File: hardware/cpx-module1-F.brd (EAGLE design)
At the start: 85.1 x 128.5 mm, 6 parts, among them T1 TOUCHPADROUND1, T2 TOUCHPADROUND1, T3 TOUCHPADROUND1, T4 TOUCHPADROUND1, U1 CIRCUITPLAYGROUNDEXPRESS

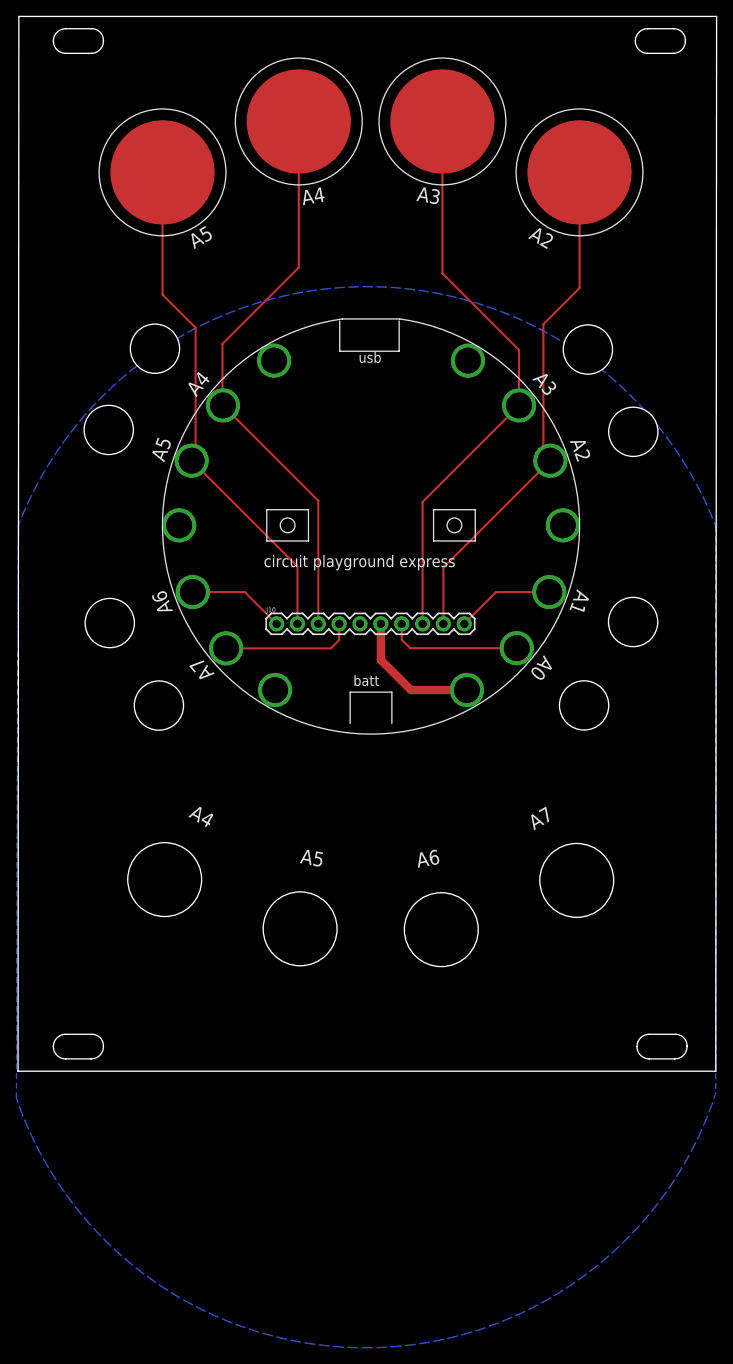
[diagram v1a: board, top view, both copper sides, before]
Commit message: added protection diodes and filter caps, added pdfs
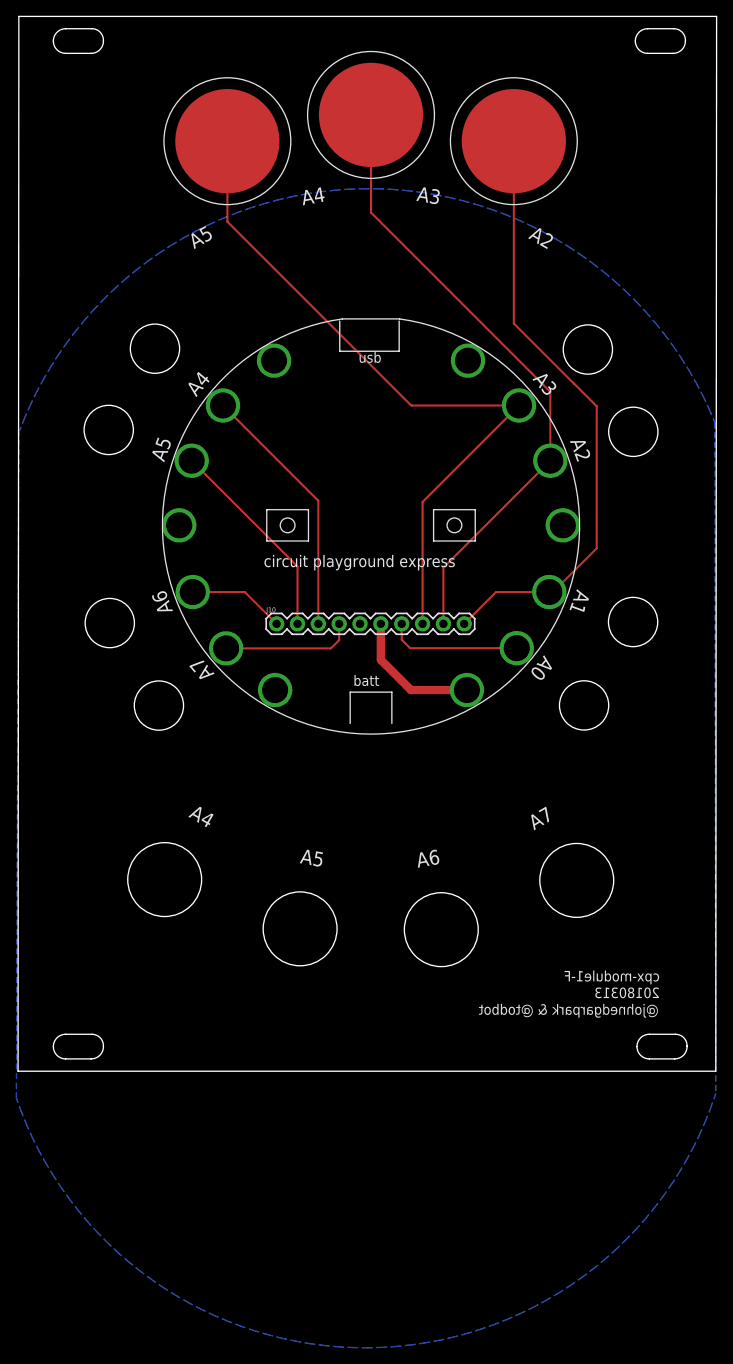
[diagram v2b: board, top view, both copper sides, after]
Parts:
- removed T3: TOUCHPADROUND1, todstuff:TOUCHPAD1
- moved T2 43.0 mm to (17.4, 50.8)
- moved T4 26.3 mm to (0.00, 54.0)
- moved T1 26.3 mm to (-17.5, 50.8)
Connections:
- net A1: now also T2.TOUCH
- net A4: no longer T3.TOUCH
- net A5: no longer T2.TOUCH
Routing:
- net A1: track 12.0 -> 73.7 mm
- net A4: track 69.9 -> 31.4 mm
- net A5: track 62.3 -> 25.2 mm
- net A3: track 69.9 -> 86.1 mm
- net A2: track 62.6 -> 76.4 mm
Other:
- board text added: "20180313"
- board text added: "@johnedgarpark & @todbot"
- board text added: "cpx-module1-F"
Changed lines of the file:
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@@
 <layer number="131" name="prix" color="7" fill="1" visible="no" active="yes"/>
 <layer number="132" name="test" color="7" fill="1" visible="no" active="yes"/>
+<layer number="133" name="Ports" color="7" fill="1" visible="no" active="yes"/>
+<layer number="134" name="Port2" color="7" fill="1" visible="no" active="yes"/>
+<layer number="135" name="Port3" color="7" fill="1" visible="no" active="yes"/>
 <layer number="144" name="Drill_legend" color="7" fill="1" visible="no" active="yes"/>
 <layer number="150" name="Notes" color="7" fill="1" visible="no" active="yes"/>
@@
 <dimension x1="46.8" y1="4" x2="43.8" y2="-62.5" x3="59.8" y3="-29.25" textsize="1.778" layer="47" dtype="vertical"/>
 <dimension x1="46.8" y1="4" x2="11.36" y2="-8" x3="45.7" y3="-2" textsize="1.778" layer="47" dtype="vertical"/>
+<text x="35.178" y="-51.555" size="1.27" layer="21" rot="MR0">cpx-module1-F</text>
+<text x="35.178" y="-53.587" size="1.27" layer="21" rot="MR0">20180313</text>
+<text x="35.051" y="-55.619" size="1.27" layer="21" rot="MR0">@johnedgarpark &amp; @todbot</text>
 </plain>
 <attributes>
@@
 <elements>
 <element name="U1" library="todstuff" library_urn="urn:adsk.eagle:library:1731349" package="CIRCUITPLAYGROUNDEXPRESS" value="CIRCUITPLAYGROUNDEXPRESS" x="0" y="4"/>
-<element name="T1" library="todstuff" library_urn="urn:adsk.eagle:library:1731349" package="TOUCHPAD1" value="TOUCHPADROUND1" x="8.7" y="53.2"/>
-<element name="T2" library="todstuff" library_urn="urn:adsk.eagle:library:1731349" package="TOUCHPAD1" value="TOUCHPADROUND1" x="-25.4" y="47"/>
-<element name="T3" library="todstuff" library_urn="urn:adsk.eagle:library:1731349" package="TOUCHPAD1" value="TOUCHPADROUND1" x="-8.8" y="53.2"/>
+<element name="T1" library="todstuff" library_urn="urn:adsk.eagle:library:1731349" package="TOUCHPAD1" value="TOUCHPADROUND1" x="-17.5" y="50.8"/>
+<element name="T2" library="todstuff" library_urn="urn:adsk.eagle:library:1731349" package="TOUCHPAD1" value="TOUCHPADROUND1" x="17.4" y="50.8"/>
 <element name="J10" library="SparkFun-Connectors" library_urn="urn:adsk.eagle:library:513" package="1X10" package3d_urn="urn:adsk.eagle:package:38157/1" value="" x="-11.5" y="-8">
 <attribute name="PROD_ID" value="CONN-11563" x="-11.5" y="-8" size="1.778" layer="27" display="off"/>
 </element>
-<element name="T4" library="todstuff" library_urn="urn:adsk.eagle:library:1731349" package="TOUCHPAD1" value="TOUCHPADROUND1" x="25.4" y="47"/>
+<element name="T4" library="todstuff" library_urn="urn:adsk.eagle:library:1731349" package="TOUCHPAD1" value="TOUCHPADROUND1" x="0" y="54"/>
 </elements>
 <signals>
@@
 <contactref element="U1" pad="GNDR"/>
 <polygon width="0.254" layer="16">
-<vertex x="-43" y="3.9" curve="-137.899658"/>
-<vertex x="42" y="3.9"/>
+<vertex x="-42.9" y="15.3" curve="-137.899658"/>
+<vertex x="41.9" y="16.5"/>
 <vertex x="42" y="-65.2" curve="-143.090816"/>
 <vertex x="-43.2" y="-65.8"/>
@@
 <signal name="A4">
 <contactref element="U1" pad="A4"/>
-<contactref element="T3" pad="TOUCH"/>
 <contactref element="J10" pad="3"/>
 <wire x1="-18.034" y1="18.605" x2="-6.42" y2="6.991" width="0.254" layer="1"/>
 <wire x1="-6.42" y1="6.991" x2="-6.42" y2="-8" width="0.254" layer="1"/>
-<wire x1="-8.8" y1="53.2" x2="-8.8" y2="35.4" width="0.254" layer="1"/>
-<wire x1="-8.8" y1="35.4" x2="-18.1" y2="26.1" width="0.254" layer="1"/>
-<wire x1="-18.1" y1="26.1" x2="-18.1" y2="18.671" width="0.254" layer="1"/>
-<wire x1="-18.1" y1="18.671" x2="-18.034" y2="18.605" width="0.254" layer="1"/>
 </signal>
 <signal name="A5">
 <contactref element="U1" pad="A5"/>
-<contactref element="T2" pad="TOUCH"/>
 <contactref element="J10" pad="2"/>
 <wire x1="-21.844" y1="11.874" x2="-8.96" y2="-1.01" width="0.254" layer="1"/>
 <wire x1="-8.96" y1="-1.01" x2="-8.96" y2="-8" width="0.254" layer="1"/>
-<wire x1="-25.4" y1="47" x2="-25.4" y2="32.1" width="0.254" layer="1"/>
-<wire x1="-21.376" y1="12.876" x2="-21.3" y2="12.8" width="0.254" layer="1"/>
-<wire x1="-21.376" y1="28.076" x2="-21.376" y2="12.876" width="0.254" layer="1"/>
-<wire x1="-25.4" y1="32.1" x2="-21.376" y2="28.076" width="0.254" layer="1"/>
-<wire x1="-21.3" y1="12.8" x2="-21.844" y2="12.256" width="0.254" layer="1"/>
-<wire x1="-21.844" y1="12.256" x2="-21.844" y2="11.874" width="0.254" layer="1"/>
 </signal>
 <signal name="A6">
@@
 <wire x1="6.28" y1="6.851" x2="6.28" y2="-8" width="0.254" layer="1"/>
 <contactref element="T1" pad="TOUCH"/>
-<wire x1="8.7" y1="53.2" x2="8.7" y2="34.7" width="0.254" layer="1"/>
-<wire x1="18.034" y1="25.366" x2="18.034" y2="18.605" width="0.254" layer="1"/>
-<wire x1="8.7" y1="34.7" x2="18.034" y2="25.366" width="0.254" layer="1"/>
+<wire x1="-17.5" y1="50.8" x2="-17.5" y2="41" width="0.254" layer="1"/>
+<wire x1="4.895" y1="18.605" x2="18.034" y2="18.605" width="0.254" layer="1"/>
+<wire x1="-17.5" y1="41" x2="4.895" y2="18.605" width="0.254" layer="1"/>
 </signal>
 <signal name="A2">
@@
 <wire x1="8.82" y1="-1.15" x2="8.82" y2="-8" width="0.254" layer="1"/>
 <contactref element="T4" pad="TOUCH"/>
-<wire x1="25.4" y1="47" x2="25.4" y2="32.9" width="0.254" layer="1"/>
-<wire x1="25.4" y1="32.9" x2="21" y2="28.5" width="0.254" layer="1"/>
-<wire x1="21" y1="28.5" x2="21" y2="12.718" width="0.254" layer="1"/>
-<wire x1="21" y1="12.718" x2="21.844" y2="11.874" width="0.254" layer="1"/>
+<wire x1="0" y1="54" x2="0" y2="42.1" width="0.254" layer="1"/>
+<wire x1="21.844" y1="20.256" x2="21.844" y2="11.874" width="0.254" layer="1"/>
+<wire x1="0" y1="42.1" x2="21.844" y2="20.256" width="0.254" layer="1"/>
 </signal>
 <signal name="A1">
@@
 <wire x1="21.717" y1="-4.128" x2="15.232" y2="-4.128" width="0.254" layer="1"/>
 <wire x1="15.232" y1="-4.128" x2="11.36" y2="-8" width="0.254" layer="1"/>
+<contactref element="T2" pad="TOUCH"/>
+<wire x1="27.5" y1="1.2" x2="22.172" y2="-4.128" width="0.254" layer="1"/>
+<wire x1="22.172" y1="-4.128" x2="21.717" y2="-4.128" width="0.254" layer="1"/>
+<wire x1="24.7029125" y1="21.277" x2="24.723" y2="21.277" width="0.254" layer="1"/>
+<wire x1="17.4" y1="50.8" x2="17.4" y2="28.5799125" width="0.254" layer="1"/>
+<wire x1="17.4" y1="28.5799125" x2="24.7029125" y2="21.277" width="0.254" layer="1"/>
+<wire x1="24.723" y1="21.277" x2="27.5" y2="18.5" width="0.254" layer="1"/>
+<wire x1="27.5" y1="18.5" x2="27.5" y2="1.2" width="0.254" layer="1"/>
 </signal>
 <signal name="A0">
